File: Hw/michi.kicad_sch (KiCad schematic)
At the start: 52 parts, among them J1 Conn_01x02, J2 Conn_Right, P1 USB_C_Plug_USB2.0, SW1 SW_Push, U1 RP2040, U2 NCP1117ST33T3G, U3 W25Q128JVS, Y1 Crystal

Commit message: Floorplan placement
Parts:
- R1, R10, R11, R12, R13, R14, R15, R16, R17, R18, R2, R21, R3, R4, R5, R6, R7, R8, R9: footprint Resistor_SMD:R_0805_2012Metric -> Resistor_SMD:R_0603_1608Metric
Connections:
- net IO10: now also J2.7 (Pin_7)
- net IO11: now also J2.8 (Pin_8)
- net IO23: now also J2.9 (Pin_9)
- net IO24: now also J2.6 (Pin_6)
- net XOUT: now also R8.1; no longer R8.2
- net at C4.2, Y1.2: now also R8.2; no longer R8.1
- net DR+: now reaches R4.1, U1.47 (USB_DP)
- net DR-: now reaches R3.1, U1.46 (USB_DM)
- no-connect marks 0 -> 3
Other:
- moved on the sheet: R8

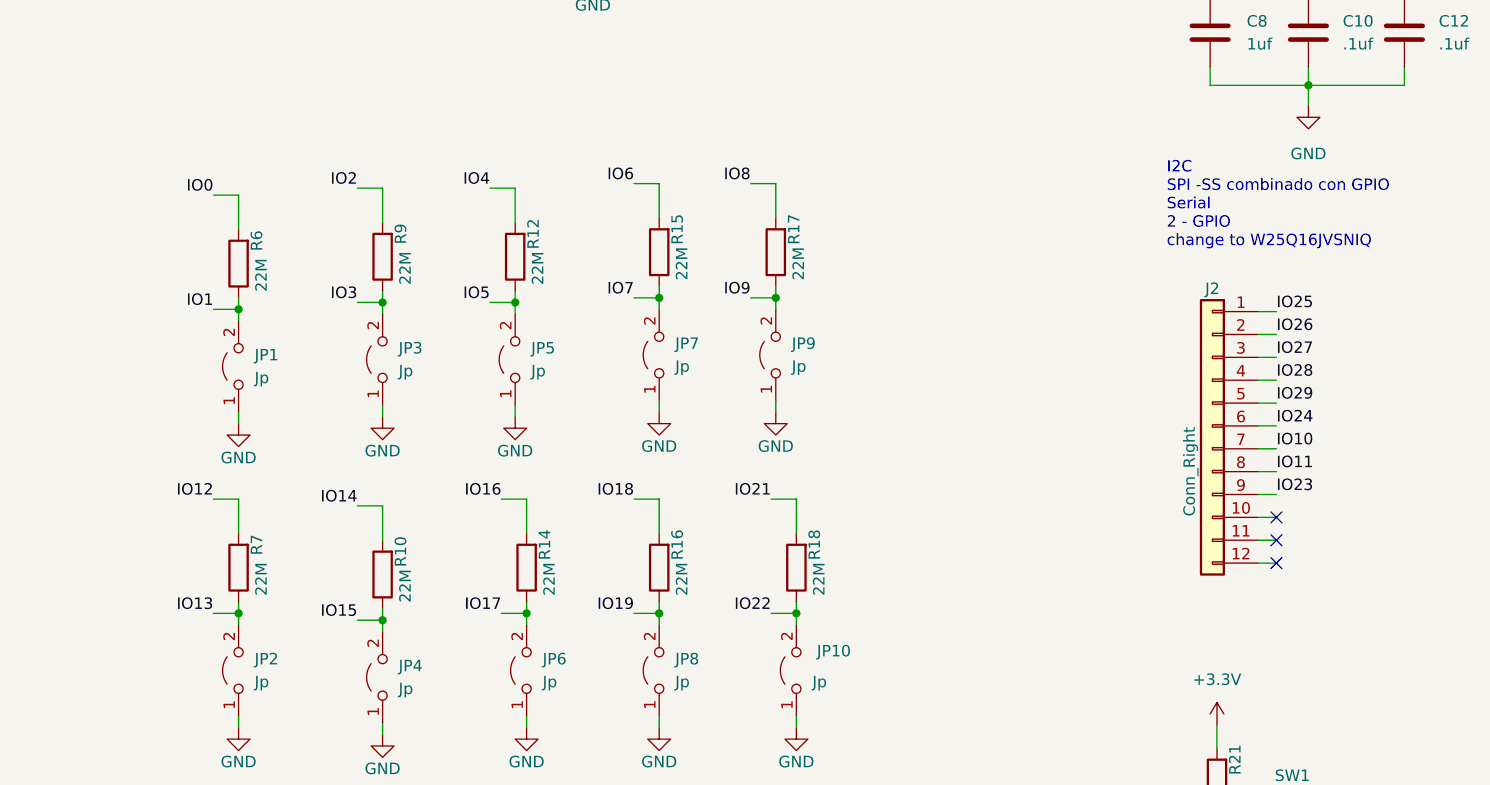
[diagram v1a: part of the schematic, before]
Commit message: Started PCB routing
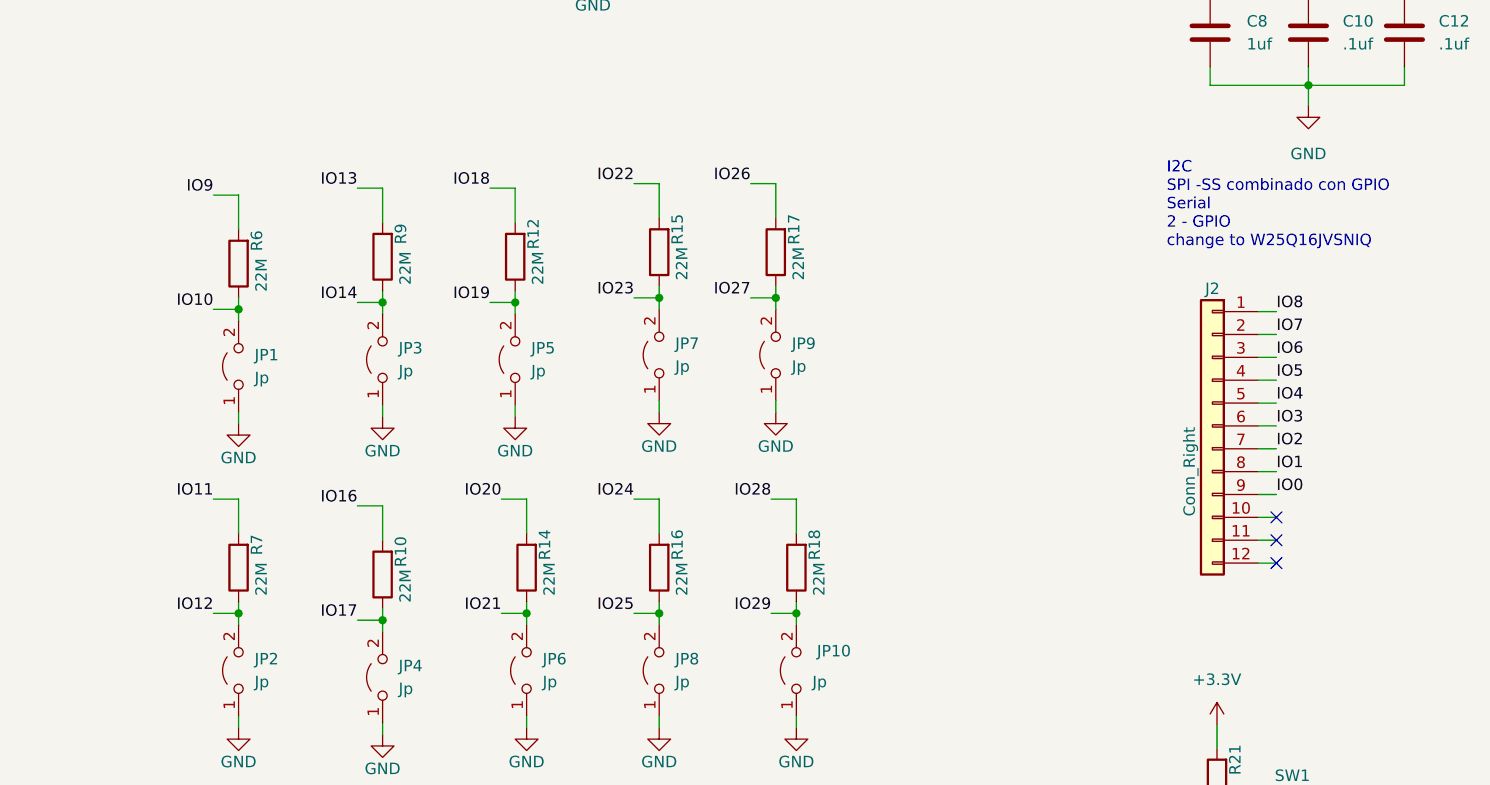
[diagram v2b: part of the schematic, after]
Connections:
- net IO0: now also J2.9 (Pin_9); no longer R6.2
- net IO1: now also J2.8 (Pin_8); no longer JP1.2 (B), R6.1
- net IO10: now also JP1.2 (B), R6.1; no longer J2.7 (Pin_7)
- net IO11: now also R7.2; no longer J2.8 (Pin_8)
- net IO12: now also JP2.2 (B), R7.1; no longer R7.2
- net IO13: now also R9.2; no longer JP2.2 (B), R7.1
- net IO14: now also JP3.2 (B), R9.1; no longer R10.2
- net IO15: no longer JP4.2 (B), R10.1
- net IO16: now also R10.2; no longer R14.2
- net IO17: now also JP4.2 (B), R10.1; no longer JP6.2 (B), R14.1
- net IO18: now also R12.2; no longer R16.2
- net IO19: now also JP5.2 (B), R12.1; no longer JP8.2 (B), R16.1
- net IO2: now also J2.7 (Pin_7); no longer R9.2
- net IO20: now also R14.2
- net IO21: now also JP6.2 (B), R14.1; no longer R18.2
- net IO22: now also R15.2; no longer JP10.2 (B), R18.1
- net IO23: now also JP7.2 (B), R15.1; no longer J2.9 (Pin_9)
- net IO24: now also R16.2; no longer J2.6 (Pin_6)
- net IO25: now also JP8.2 (B), R16.1; no longer J2.1 (Pin_1)
- net IO26: now also R17.2; no longer J2.2 (Pin_2)
- net IO27: now also JP9.2 (B), R17.1; no longer J2.3 (Pin_3)
- net IO28: now also R18.2; no longer J2.4 (Pin_4)
- net IO29: now also JP10.2 (B), R18.1; no longer J2.5 (Pin_5)
- net IO3: now also J2.6 (Pin_6); no longer JP3.2 (B), R9.1
- net IO4: now also J2.5 (Pin_5); no longer R12.2
- net IO5: now also J2.4 (Pin_4); no longer JP5.2 (B), R12.1
- net IO6: now also J2.3 (Pin_3); no longer R15.2
- net IO7: now also J2.2 (Pin_2); no longer JP7.2 (B), R15.1
- net IO8: now also J2.1 (Pin_1); no longer R17.2
- net IO9: now also R6.2; no longer JP9.2 (B), R17.1
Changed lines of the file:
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@@
     (effects (font (size 1.27 1.27)) (justify left bottom))
   )
-  (label "IO25" (at 243.078 92.964 0)
+  (label "IO8" (at 243.078 92.964 0)
     (effects (font (size 1.27 1.27)) (justify left bottom))
   )
@@
     (effects (font (size 1.27 1.27)) (justify left bottom))
   )
-  (label "IO5" (at 155.702 91.948 180)
+  (label "IO19" (at 155.702 91.948 180)
     (effects (font (size 1.27 1.27)) (justify right bottom))
   )
@@
     (effects (font (size 1.27 1.27)) (justify left bottom))
   )
-  (label "IO12" (at 124.968 113.792 180)
-    (effects (font (size 1.27 1.27)) (justify right bottom))
-  )
-  (label "IO6" (at 171.704 78.74 180)
+  (label "IO11" (at 124.968 113.792 180)
+    (effects (font (size 1.27 1.27)) (justify right bottom))
+  )
+  (label "IO22" (at 171.704 78.74 180)
     (effects (font (size 1.27 1.27)) (justify right bottom))
   )
@@
     (effects (font (size 1.27 1.27)) (justify left bottom))
   )
-  (label "IO17" (at 156.972 126.492 180)
+  (label "IO21" (at 156.972 126.492 180)
     (effects (font (size 1.27 1.27)) (justify right bottom))
   )
@@
     (effects (font (size 1.27 1.27)) (justify right bottom))
   )
-  (label "IO16" (at 156.972 113.792 180)
+  (label "IO20" (at 156.972 113.792 180)
     (effects (font (size 1.27 1.27)) (justify right bottom))
   )
@@
     (effects (font (size 1.27 1.27)) (justify left bottom))
   )
-  (label "IO29" (at 243.078 103.124 0)
+  (label "IO4" (at 243.078 103.124 0)
     (effects (font (size 1.27 1.27)) (justify left bottom))
   )
@@
     (effects (font (size 1.27 1.27)) (justify right bottom))
   )
-  (label "IO1" (at 124.968 92.71 180)
+  (label "IO10" (at 124.968 92.71 180)
     (effects (font (size 1.27 1.27)) (justify right bottom))
   )
@@
     (effects (font (size 1.27 1.27)) (justify right bottom))
   )
-  (label "IO26" (at 243.078 95.504 0)
+  (label "IO7" (at 243.078 95.504 0)
     (effects (font (size 1.27 1.27)) (justify left bottom))
   )
@@
     (effects (font (size 1.27 1.27)) (justify left bottom))
   )
-  (label "IO9" (at 184.658 91.44 180)
-    (effects (font (size 1.27 1.27)) (justify right bottom))
-  )
-  (label "IO28" (at 243.078 100.584 0)
+  (label "IO27" (at 184.658 91.44 180)
+    (effects (font (size 1.27 1.27)) (justify right bottom))
+  )
+  (label "IO5" (at 243.078 100.584 0)
     (effects (font (size 1.27 1.27)) (justify left bottom))
   )
@@
     (effects (font (size 1.27 1.27)) (justify right bottom))
   )
-  (label "IO11" (at 243.078 110.744 0)
-    (effects (font (size 1.27 1.27)) (justify left bottom))
-  )
-  (label "IO27" (at 243.078 98.044 0)
+  (label "IO1" (at 243.078 110.744 0)
+    (effects (font (size 1.27 1.27)) (justify left bottom))
+  )
+  (label "IO6" (at 243.078 98.044 0)
     (effects (font (size 1.27 1.27)) (justify left bottom))
   )
@@
     (effects (font (size 1.27 1.27)) (justify right bottom))
   )
-  (label "IO22" (at 186.944 126.492 180)
+  (label "IO29" (at 186.944 126.492 180)
     (effects (font (size 1.27 1.27)) (justify right bottom))
   )
@@
     (effects (font (size 1.27 1.27)) (justify left bottom))
   )
-  (label "IO2" (at 140.97 79.248 180)
-    (effects (font (size 1.27 1.27)) (justify right bottom))
-  )
-  (label "IO8" (at 184.658 78.74 180)
-    (effects (font (size 1.27 1.27)) (justify right bottom))
-  )
-  (label "IO14" (at 140.97 114.554 180)
+  (label "IO13" (at 140.97 79.248 180)
+    (effects (font (size 1.27 1.27)) (justify right bottom))
+  )
+  (label "IO26" (at 184.658 78.74 180)
+    (effects (font (size 1.27 1.27)) (justify right bottom))
+  )
+  (label "IO16" (at 140.97 114.554 180)
     (effects (font (size 1.27 1.27)) (justify right bottom))
   )
@@
     (effects (font (size 1.27 1.27)) (justify right bottom))
   )
-  (label "IO18" (at 171.704 113.792 180)
-    (effects (font (size 1.27 1.27)) (justify right bottom))
-  )
-  (label "IO19" (at 171.704 126.492 180)
-    (effects (font (size 1.27 1.27)) (justify right bottom))
-  )
-  (label "IO24" (at 243.078 105.664 0)
+  (label "IO24" (at 171.704 113.792 180)
+    (effects (font (size 1.27 1.27)) (justify right bottom))
+  )
+  (label "IO25" (at 171.704 126.492 180)
+    (effects (font (size 1.27 1.27)) (justify right bottom))
+  )
+  (label "IO3" (at 243.078 105.664 0)
     (effects (font (size 1.27 1.27)) (justify left bottom))
   )
@@
     (effects (font (size 1.27 1.27)) (justify left bottom))
   )
-  (label "IO0" (at 124.968 80.01 180)
+  (label "IO9" (at 124.968 80.01 180)
     (effects (font (size 1.27 1.27)) (justify right bottom))
   )
@@
     (effects (font (size 1.27 1.27)) (justify left bottom))
   )
-  (label "IO7" (at 171.704 91.44 180)
+  (label "IO23" (at 171.704 91.44 180)
     (effects (font (size 1.27 1.27)) (justify right bottom))
   )
@@
     (effects (font (size 1.27 1.27)) (justify right bottom))
   )
-  (label "IO13" (at 124.968 126.492 180)
-    (effects (font (size 1.27 1.27)) (justify right bottom))
-  )
-  (label "IO23" (at 243.078 113.284 0)
-    (effects (font (size 1.27 1.27)) (justify left bottom))
-  )
-  (label "IO15" (at 140.97 127.254 180)
+  (label "IO12" (at 124.968 126.492 180)
+    (effects (font (size 1.27 1.27)) (justify right bottom))
+  )
+  (label "IO0" (at 243.078 113.284 0)
+    (effects (font (size 1.27 1.27)) (justify left bottom))
+  )
+  (label "IO17" (at 140.97 127.254 180)
     (effects (font (size 1.27 1.27)) (justify right bottom))
   )
@@
     (effects (font (size 1.27 1.27)) (justify left bottom))
   )
-  (label "IO4" (at 155.702 79.248 180)
-    (effects (font (size 1.27 1.27)) (justify right bottom))
-  )
-  (label "IO21" (at 186.944 113.792 180)
+  (label "IO18" (at 155.702 79.248 180)
+    (effects (font (size 1.27 1.27)) (justify right bottom))
+  )
+  (label "IO28" (at 186.944 113.792 180)
     (effects (font (size 1.27 1.27)) (justify right bottom))
   )
@@
     (effects (font (size 1.27 1.27)) (justify left bottom))
   )
-  (label "IO10" (at 243.078 108.204 0)
+  (label "IO2" (at 243.078 108.204 0)
     (effects (font (size 1.27 1.27)) (justify left bottom))
   )
@@
     (effects (font (size 1.27 1.27)) (justify right bottom))
   )
-  (label "IO3" (at 140.97 91.948 180)
-    (effects (font (size 1.27 1.27)) (justify right bottom))
-  )
+  (label "IO14" (at 140.97 91.948 180)
+    (effects (font (size 1.27 1.27)) (justify right bottom))
+  )

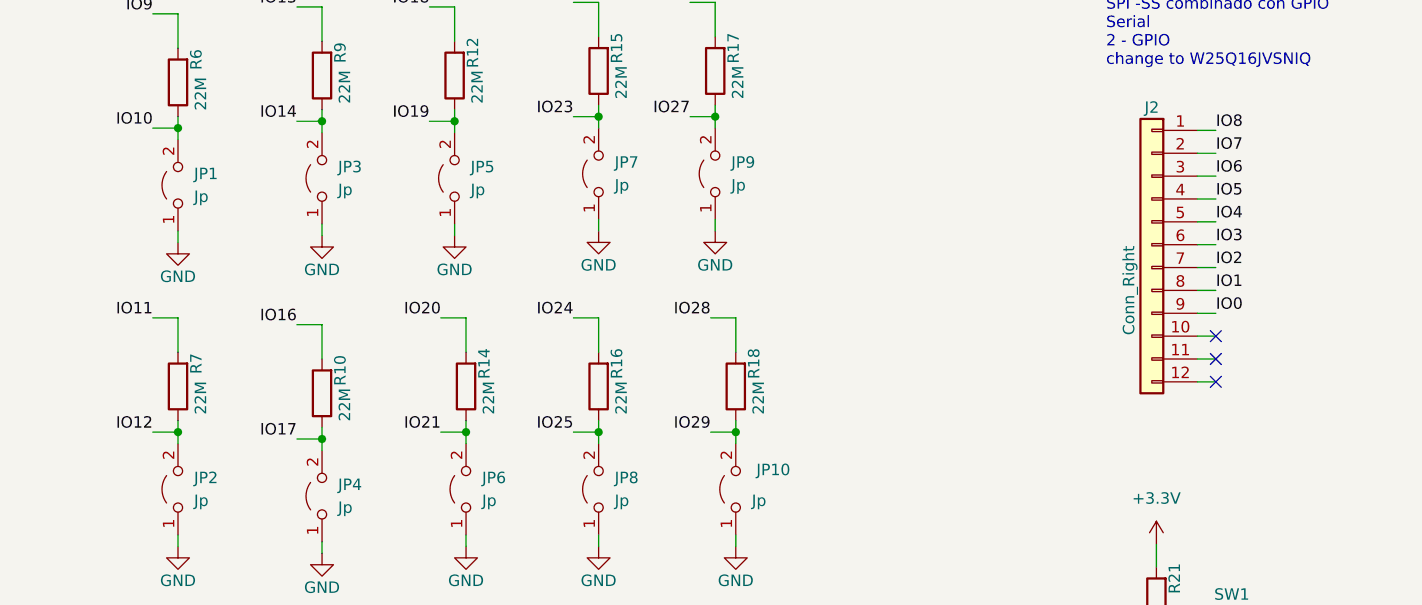
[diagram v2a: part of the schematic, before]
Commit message: Resisitive sensors connected
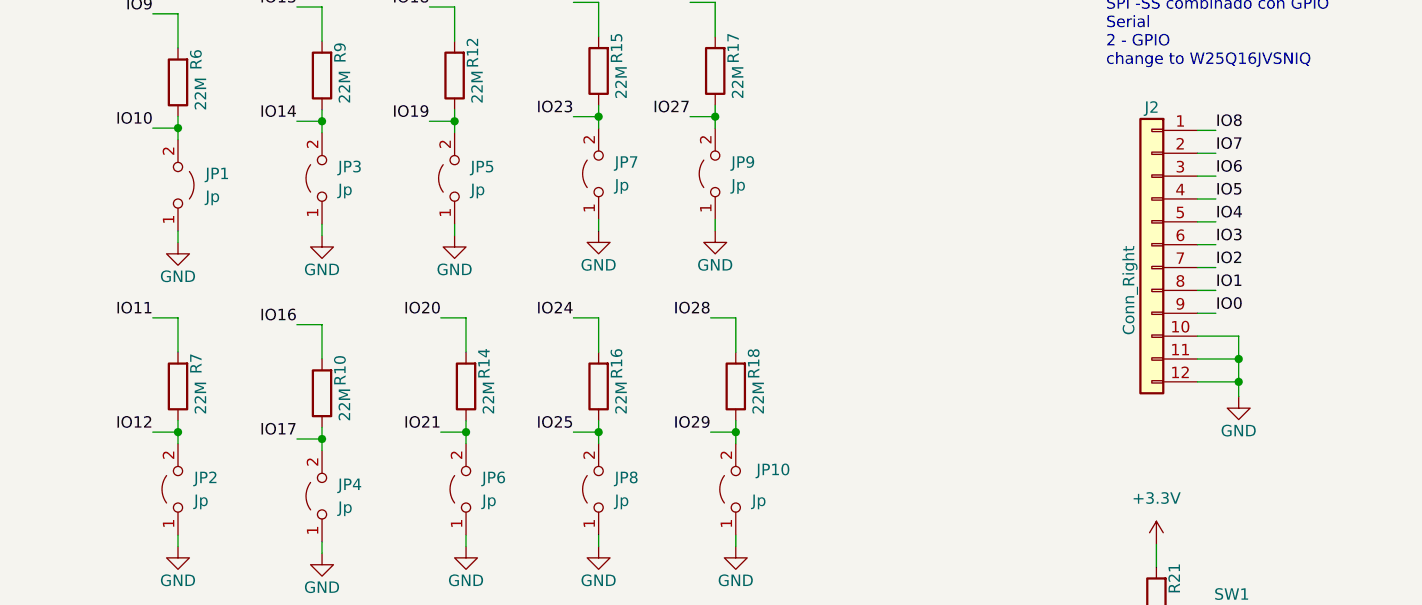
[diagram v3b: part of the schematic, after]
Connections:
- net GND: now also J2.10 (Pin_10), J2.11 (Pin_11), J2.12 (Pin_12)
- no-connect marks 3 -> 0
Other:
- moved on the sheet: JP1
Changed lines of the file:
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@@
   (junction (at 230.124 38.608) (diameter 0) (color 0 0 0 0)
   )
+  (junction (at 245.618 118.364) (diameter 0) (color 0 0 0 0)
+  )
   (junction (at 236.474 152.908) (diameter 0) (color 0 0 0 0)
   )
+  (junction (at 245.618 120.904) (diameter 0) (color 0 0 0 0)
+  )
   (junction (at 28.702 63.754) (diameter 0) (color 0 0 0 0)
   )
@@
   (junction (at 246.888 38.608) (diameter 0) (color 0 0 0 0)
   )
-  (no_connect (at 243.078 120.904))
-  (no_connect (at 243.078 115.824))
-  (no_connect (at 243.078 118.364))
   (wire (pts (xy 246.634 67.818) (xy 235.712 67.818))
     (stroke (width 0) (type default) (color 0 0 0 0))
@@
     (stroke (width 0) (type default) (color 0 0 0 0))
   )
-  (wire (pts (xy 241.046 115.824) (xy 243.078 115.824))
+  (wire (pts (xy 241.046 115.824) (xy 245.618 115.824))
     (stroke (width 0) (type default) (color 0 0 0 0))
   )
@@
     (stroke (width 0) (type default) (color 0 0 0 0))
   )
-  (wire (pts (xy 241.046 118.364) (xy 243.078 118.364))
+  (wire (pts (xy 245.618 120.904) (xy 245.618 122.555))
+    (stroke (width 0) (type default) (color 0 0 0 0))
+  )
+  (wire (pts (xy 241.046 118.364) (xy 245.618 118.364))
     (stroke (width 0) (type default) (color 0 0 0 0))
   )
@@
     (stroke (width 0) (type default) (color 0 0 0 0))
   )
+  (wire (pts (xy 245.618 118.364) (xy 245.618 115.824))
+    (stroke (width 0) (type default) (color 0 0 0 0))
+  )
   (wire (pts (xy 143.764 118.364) (xy 143.764 114.554))
     (stroke (width 0) (type default) (color 0 0 0 0))
@@
     (stroke (width 0) (type default) (color 0 0 0 0))
   )
+  (wire (pts (xy 245.618 120.904) (xy 245.618 118.364))
+    (stroke (width 0) (type default) (color 0 0 0 0))
+  )
   (wire (pts (xy 158.496 91.948) (xy 158.496 93.218))
     (stroke (width 0) (type default) (color 0 0 0 0))
@@
     (stroke (width 0) (type default) (color 0 0 0 0))
   )
-  (wire (pts (xy 241.046 120.904) (xy 243.078 120.904))
+  (wire (pts (xy 241.046 120.904) (xy 245.618 120.904))
     (stroke (width 0) (type default) (color 0 0 0 0))
   )
@@
     (pin "2")
   )
-  (symbol (lib_id "Jumper:Jumper_2_Open") (at 127.762 99.06 90) (unit 1)
-    (in_bom yes) (on_board yes) (fields_autoplaced)
-    (property "Reference" "JP1" (id 0) (at 129.54 97.7899 90)
-      (effects (font (size 1.27 1.27)) (justify right))
-    )
-    (property "Value" "Jp" (id 1) (at 129.54 100.3299 90)
-      (effects (font (size 1.27 1.27)) (justify right))
+  (symbol (lib_id "Jumper:Jumper_2_Open") (at 127.762 99.06 270) (mirror x) (unit 1)
+    (in_bom yes) (on_board yes) (fields_autoplaced)
+    (property "Reference" "JP1" (id 0) (at 130.81 97.7899 90)
+      (effects (font (size 1.27 1.27)) (justify left))
+    )
+    (property "Value" "Jp" (id 1) (at 130.81 100.3299 90)
+      (effects (font (size 1.27 1.27)) (justify left))
     )
     (property "Footprint" "" (id 2) (at 127.762 99.06 0)
@@
     (pin "1")
     (pin "2")
+  )
+  (symbol (lib_id "power:GND") (at 245.618 122.555 0) (unit 1)
+    (in_bom yes) (on_board yes)
+    (property "Reference" "#PWR?" (id 0) (at 245.618 128.905 0)
+      (effects (font (size 1.27 1.27)) hide)
+    )
+    (property "Value" "GND" (id 1) (at 245.618 126.365 0))
+    (property "Footprint" "" (id 2) (at 245.618 122.555 0)
+      (effects (font (size 1.27 1.27)) hide)
+    )
+    (property "Datasheet" "" (id 3) (at 245.618 122.555 0)
+      (effects (font (size 1.27 1.27)) hide)
+    )
+    (pin "1")
   )
   (symbol (lib_id "power:GND") (at 189.738 139.192 0) (unit 1)
@@
       (reference "#PWR0102") (unit 1) (value "+3.3V") (footprint "")
     )
+    (path "/51922175-4c44-4a31-bb11-efc74e3866fe"
+      (reference "#PWR?") (unit 1) (value "GND") (footprint "")
+    )
     (path "/6c00fb26-6a97-4b66-9ca0-7145f81dd24b"
